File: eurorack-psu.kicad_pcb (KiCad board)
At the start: 2 copper layers, 109.3 x 62 mm, 30 parts, among them J1 Conn_02x08_Odd_Even, U1 LM317, U2 LM337

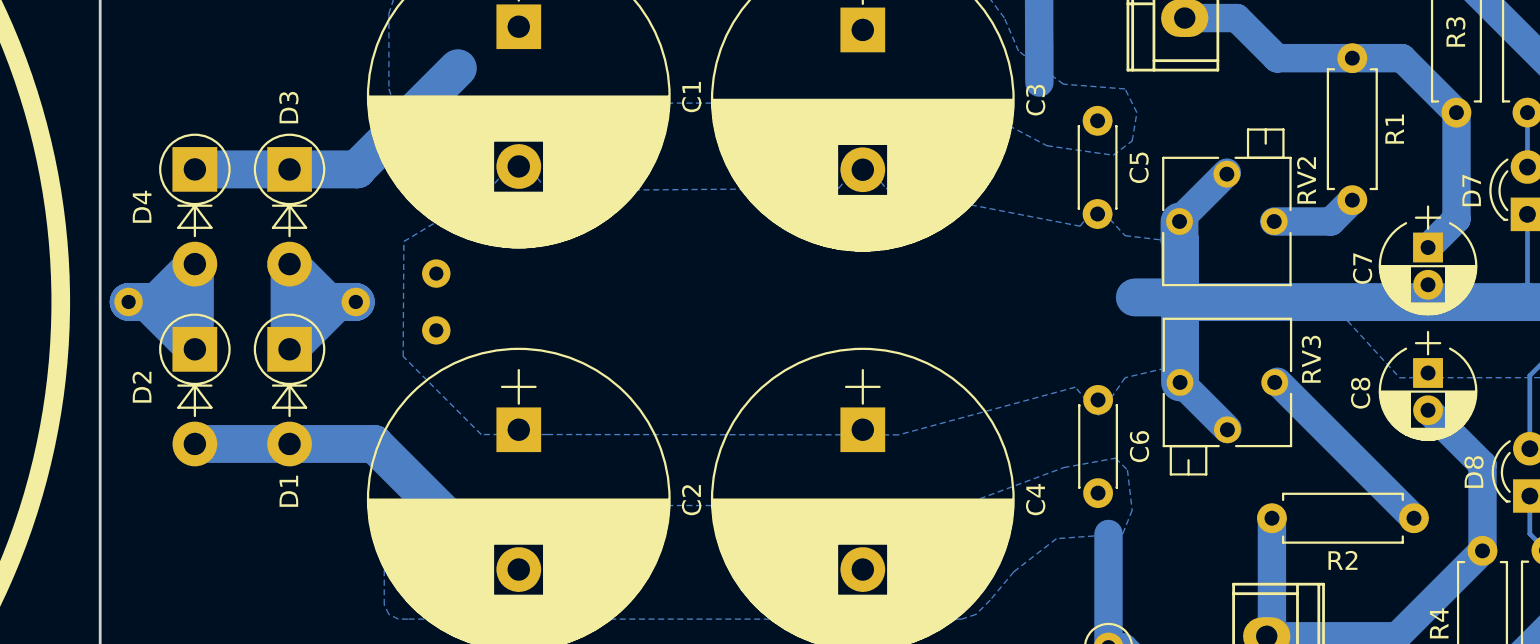
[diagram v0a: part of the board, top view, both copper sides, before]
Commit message: use new txfmr footprint, move trimmers further apart
the trimmers were colliding (footprint outline is too small) and txfmr
leads are too thick to fit through the default sized vias
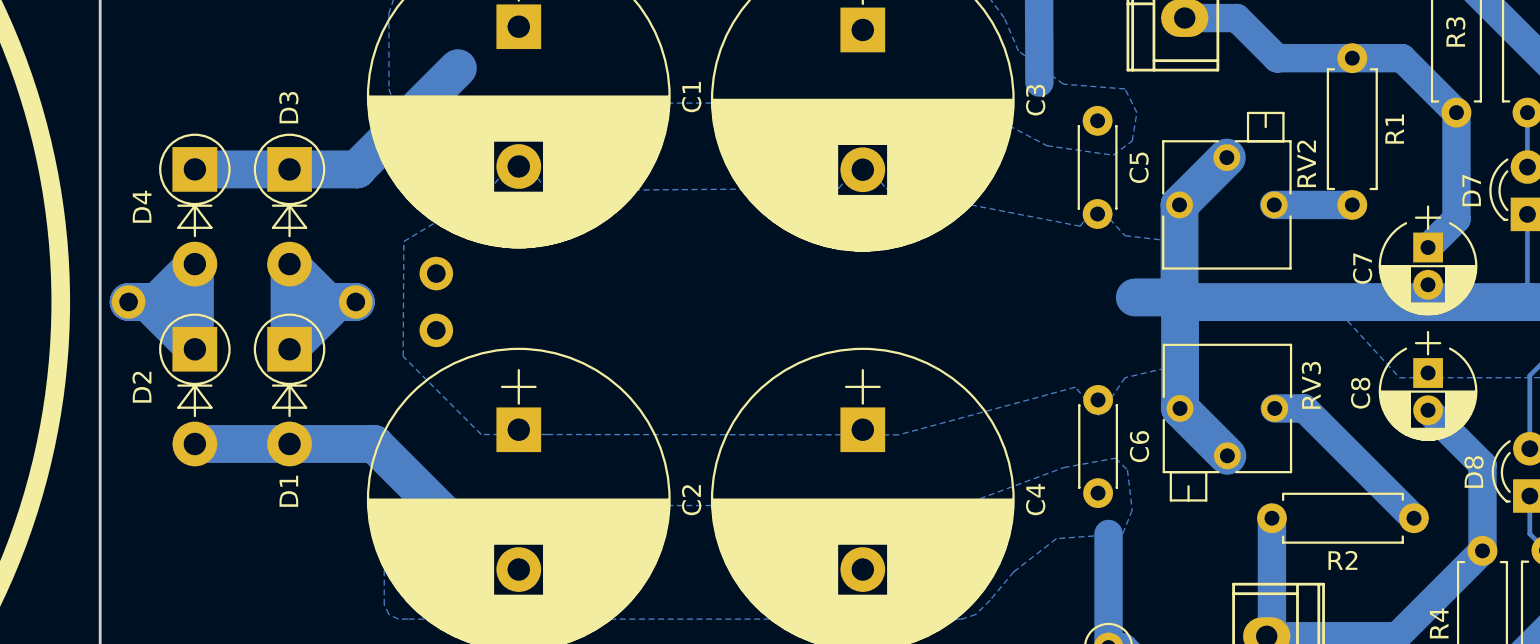
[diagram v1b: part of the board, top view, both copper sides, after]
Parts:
- moved RV3 1.40 mm to (188.5, 97.4)
- moved RV2 0.89 mm to (193.5, 86.5)
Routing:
- net GNDREF: track 75.5 -> 77.8 mm
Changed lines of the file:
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@@
     (thickness 1.6)
     (drawings 4)
-    (tracks 101)
+    (tracks 100)
     (zones 0)
     (modules 30)
@@
   )
   (setup
-    (last_trace_width 0.25)
+    (last_trace_width 2.032)
     (user_trace_width 0.508)
     (user_trace_width 1.016)
@@
     (mod_text_size 1 1)
     (mod_text_width 0.15)
-    (pad_size 1.524 1.524)
-    (pad_drill 0.762)
+    (pad_size 1.6 1.6)
+    (pad_drill 0.8)
     (pad_to_mask_clearance 0.051)
     (solder_mask_min_width 0.25)
@@
     )
     (fp_circle (center 0 0) (end 37 0) (layer F.SilkS) (width 1))
-    (pad 5 thru_hole circle (at 0 40.64 90) (size 1.524 1.524) (drill 0.762) (layers *.Cu *.Mask)
+    (pad 5 thru_hole circle (at 0 40.64 90) (size 1.8 1.8) (drill 1) (layers *.Cu *.Mask)
       (net 9 "Net-(D2-Pad1)"))
-    (pad 6 thru_hole circle (at 1.524 57.15 90) (size 1.524 1.524) (drill 0.762) (layers *.Cu *.Mask)
+    (pad 6 thru_hole circle (at 1.524 57.15 90) (size 1.8 1.8) (drill 1) (layers *.Cu *.Mask)
       (net 1 GNDREF))
-    (pad 7 thru_hole circle (at -1.524 57.15 90) (size 1.524 1.524) (drill 0.762) (layers *.Cu *.Mask)
+    (pad 7 thru_hole circle (at -1.524 57.15 90) (size 1.8 1.8) (drill 1) (layers *.Cu *.Mask)
       (net 1 GNDREF))
-    (pad 8 thru_hole circle (at 0 52.832 90) (size 1.524 1.524) (drill 0.762) (layers *.Cu *.Mask)
+    (pad 8 thru_hole circle (at 0 52.832 90) (size 1.8 1.8) (drill 1) (layers *.Cu *.Mask)
       (net 8 "Net-(D1-Pad1)"))
   )
@@
   )
   (module Potentiometers:Potentiometer_Trimmer_Bourns_3266P (layer F.Cu)
-    (at 193.548 87.376 270)
+    (at 193.548 86.487 270)
     (descr "Spindle Trimmer Potentiometer, Bourns 3266P, https://www.bourns.com/pdfs/3266.pdf")
     (tags "Spindle Trimmer Potentiometer   Bourns 3266P")
@@
   )
   (module Potentiometers:Potentiometer_Trimmer_Bourns_3266P (layer F.Cu)
-    (at 188.497 96.012 90)
+    (at 188.497 97.409 90)
     (descr "Spindle Trimmer Potentiometer, Bourns 3266P, https://www.bourns.com/pdfs/3266.pdf")
     (tags "Spindle Trimmer Potentiometer   Bourns 3266P")
@@
     (pad 1 thru_hole circle (at 0 0 270) (size 1.6 1.6) (drill 0.8) (layers *.Cu *.Mask)
       (net 4 "Net-(C7-Pad1)"))
-    (pad 2 thru_hole oval (at 7.62 0 270) (size 1.6 1.6) (drill 0.8) (layers *.Cu *.Mask)
+    (pad 2 thru_hole oval (at 7.874 0 270) (size 1.6 1.6) (drill 0.8) (layers *.Cu *.Mask)
       (net 12 "Net-(R1-Pad2)"))
     (model ${KISYS3DMOD}/Resistors_THT.3dshapes/R_Axial_DIN0207_L6.3mm_D2.5mm_P7.62mm_Horizontal.wrl
@@
   (via (at 183.747 73.92) (size 1.524) (drill 1.19888) (layers F.Cu B.Cu) (net 0))
   (segment (start 171.3 84.425) (end 171.475 84.6) (width 0.25) (layer B.Cu) (net 1) (status 30))
-  (segment (start 188.467 87.295) (end 191.007 84.755) (width 1.524) (layer B.Cu) (net 1) (status 30))
   (segment (start 208.922 91.7) (end 212.472 88.15) (width 1.524) (layer B.Cu) (net 1) (status 20))
-  (segment (start 188.497 95.972) (end 191.037 98.512) (width 1.524) (layer B.Cu) (net 1) (status 30))
   (segment (start 220.107 95.275) (end 220.207 95.375) (width 1.524) (layer B.Cu) (net 1) (status 30))
   (segment (start 220.207 95.375) (end 220.207 97.915) (width 1.524) (layer B.Cu) (net 1) (status 30))
@@
   (segment (start 188.467 91.452) (end 188.715 91.7) (width 2.032) (layer B.Cu) (net 1))
   (segment (start 188.467 91.452) (end 186.067 91.452) (width 2.032) (layer B.Cu) (net 1))
-  (segment (start 188.497 91.482) (end 188.467 91.452) (width 2.032) (layer B.Cu) (net 1))
-  (segment (start 188.497 96.012) (end 188.497 91.482) (width 2.032) (layer B.Cu) (net 1) (status 10))
-  (segment (start 188.468 88.394233) (end 188.497 88.423233) (width 2.032) (layer B.Cu) (net 1))
-  (segment (start 188.497 88.423233) (end 188.497 91.482) (width 2.032) (layer B.Cu) (net 1))
-  (segment (start 188.468 87.376) (end 188.468 88.394233) (width 2.032) (layer B.Cu) (net 1) (status 10))
   (segment (start 207.264 95.645) (end 208.922 93.987) (width 0.25) (layer B.Cu) (net 1))
   (segment (start 207.264 99.568) (end 207.264 95.645) (width 0.25) (layer B.Cu) (net 1) (status 10))
   (segment (start 207.137 86.995) (end 207.137 91.7) (width 0.25) (layer B.Cu) (net 1) (status 10))
   (segment (start 207.137 91.7) (end 208.922 91.7) (width 2.032) (layer B.Cu) (net 1))
+  (segment (start 188.468 91.453) (end 188.497 91.482) (width 2.032) (layer B.Cu) (net 1))
+  (segment (start 188.468 86.487) (end 188.468 91.453) (width 2.032) (layer B.Cu) (net 1))
+  (segment (start 188.468 86.487) (end 191.008 83.947) (width 2.032) (layer B.Cu) (net 1))
+  (segment (start 188.497 91.482) (end 188.467 91.452) (width 2.032) (layer B.Cu) (net 1))
+  (segment (start 188.497 97.409) (end 188.497 91.482) (width 2.032) (layer B.Cu) (net 1))
+  (segment (start 188.497 97.409) (end 191.037 99.949) (width 2.032) (layer B.Cu) (net 1))
   (segment (start 152.175 77.1) (end 152 76.925) (width 0.25) (layer B.Cu) (net 2) (status 30))
   (segment (start 140.716 84.582) (end 144.343 84.582) (width 2.032) (layer B.Cu) (net 2) (status 10))
@@
   (segment (start 207.264 104.14) (end 208.153 105.029) (width 0.25) (layer B.Cu) (net 11) (status 20))
   (segment (start 207.264 102.108) (end 207.264 104.14) (width 0.25) (layer B.Cu) (net 11) (status 10))
-  (segment (start 196.596 87.376) (end 197.739 86.233) (width 1.524) (layer B.Cu) (net 12) (status 20))
-  (segment (start 193.548 87.376) (end 196.596 87.376) (width 1.524) (layer B.Cu) (net 12) (status 10))
-  (segment (start 193.722 95.972) (end 201.047 103.297) (width 1.524) (layer B.Cu) (net 13) (status 30))
+  (segment (start 193.548 86.487) (end 197.739 86.487) (width 1.524) (layer B.Cu) (net 12))
+  (segment (start 195.159 97.409) (end 201.047 103.297) (width 1.524) (layer B.Cu) (net 13))
+  (segment (start 193.577 97.409) (end 195.159 97.409) (width 1.524) (layer B.Cu) (net 13))
   (segment (start 220.207 87.755) (end 222.747 87.755) (width 1.524) (layer B.Cu) (net 14) (status 30))
   (segment (start 220.207 85.215) (end 222.747 85.215) (width 1.524) (layer B.Cu) (net 15) (status 30))
